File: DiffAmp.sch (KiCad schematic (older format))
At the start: 81 parts, among them J1 USB_OTG, J2 Conn_01x01_Female, J3 Conn_01x01_Female, J4 Conn_01x01_Female, J5 CONN_01X05, J6 Conn_01x01_Female, J7 Conn_01x01_Female, Q1 Q_NMOS_GSD, SW1 NR01105, U1 PIC12F1572-IMS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

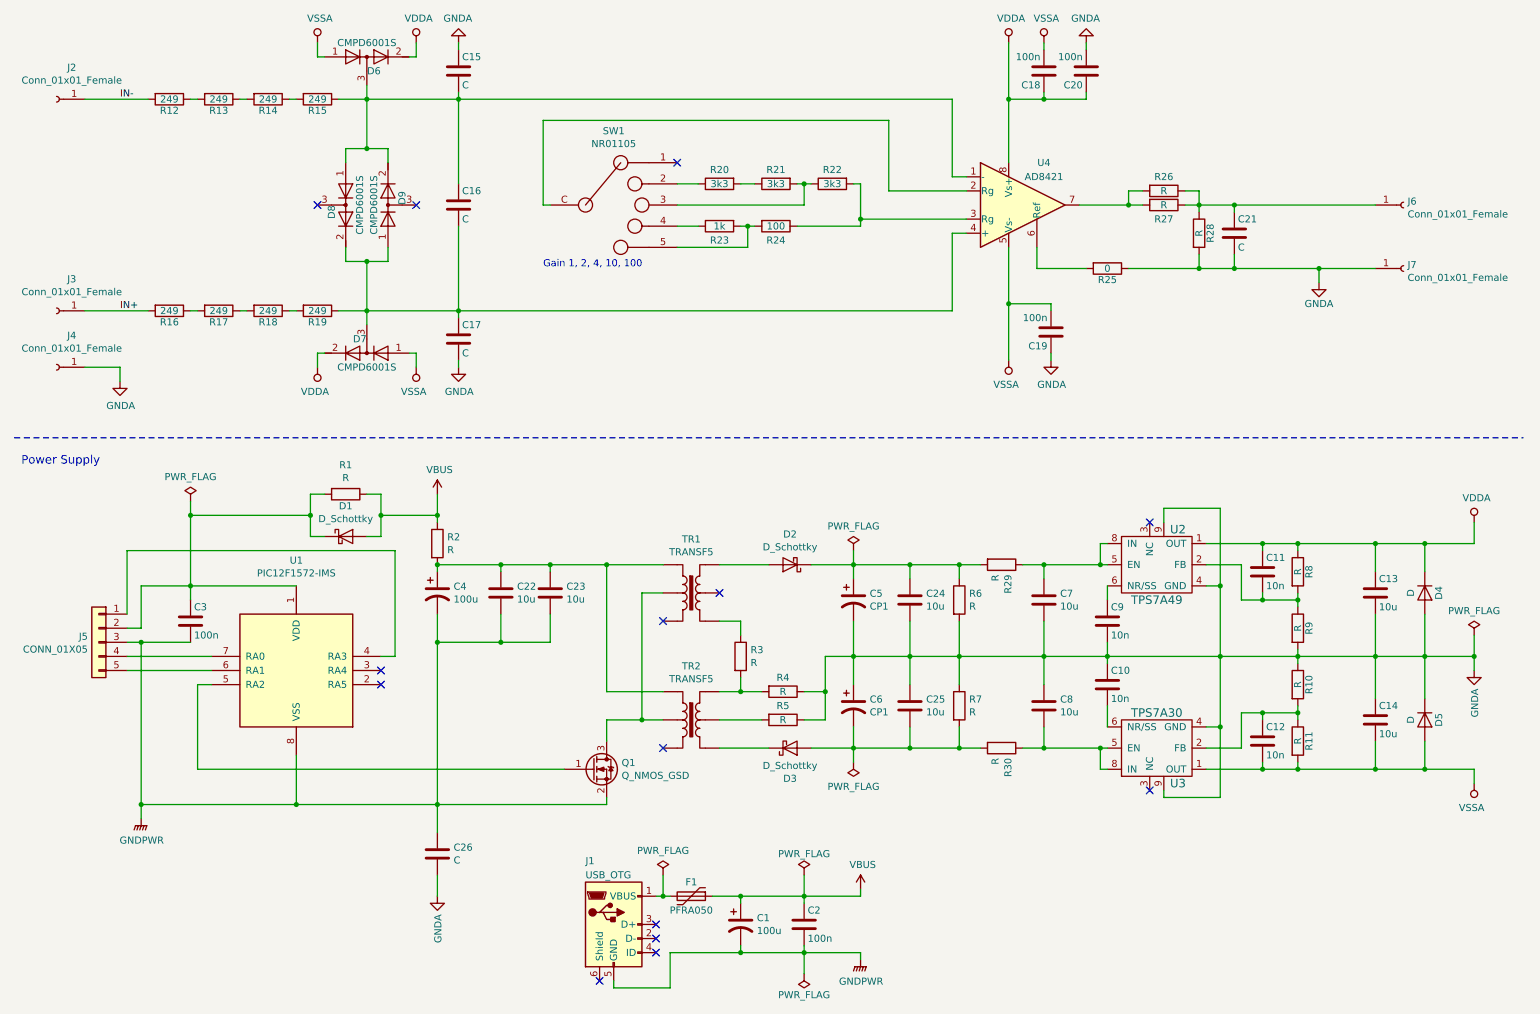
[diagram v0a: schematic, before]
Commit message: Changes in first assembly added to schematic
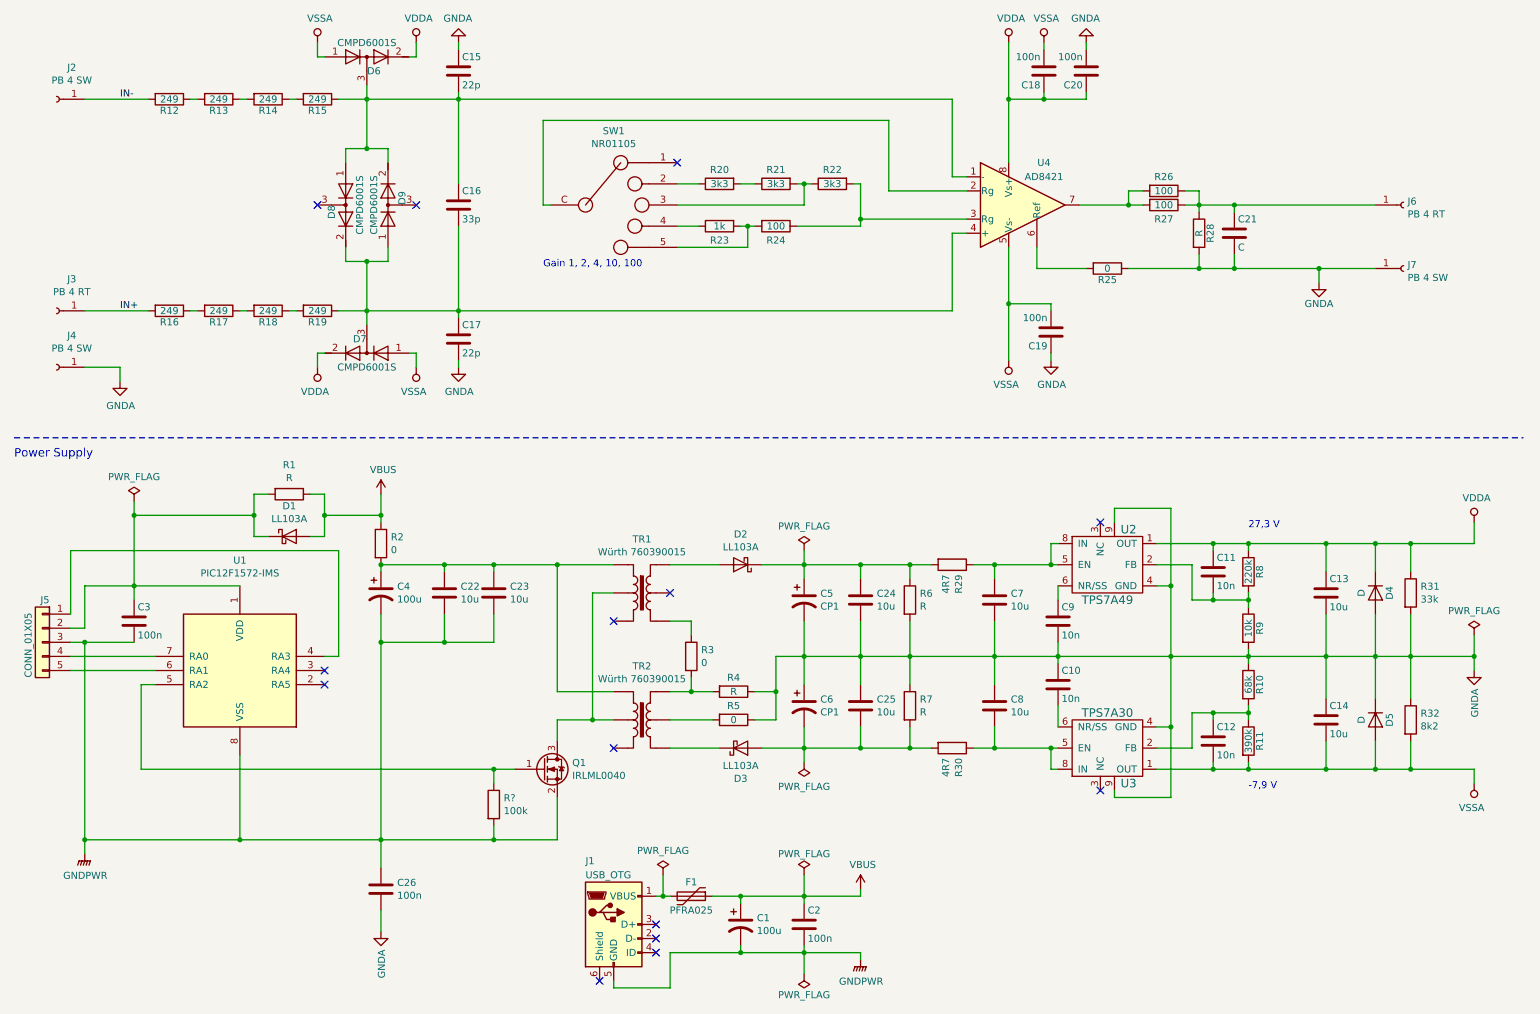
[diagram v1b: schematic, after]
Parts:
- added R31: 33k, Resistors_SMD:R_0805, symbol Device:R
- added R32: 8k2, Resistors_SMD:R_0805, symbol Device:R
- added R?: 100k, Resistors_SMD:R_0805, symbol Device:R
- C15, C17: value C -> 22p
- C16: value C -> 33p
- C26: value C -> 100n
- D1, D2, D3: value D_Schottky -> LL103A
- F1: value PFRA050 -> PFRA025
- J2, J4, J7: value Conn_01x01_Female -> PB 4 SW
- J3, J6: value Conn_01x01_Female -> PB 4 RT
- Q1: value Q_NMOS_GSD -> IRLML0040
- R10: value R -> 68k
- R11: value R -> 390k
- R2, R3, R5: value R -> 0
- R26, R27: value R -> 100
- R29, R30: value R -> 4R7
- R8: value R -> 220k
- R9: value R -> 10k
- TR1, TR2: value TRANSF5 -> Würth 760390015
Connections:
- net GNDA: now also R31.2, R32.1
- net GNDPWR: now also R?.2
- net VDDA: now also R31.1
- net VSSA: now also R32.2
- net at Q1.1 (G), U1.5 (RA2): now also R?.1
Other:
- note added: "-7,9 V"
- note added: "27,3 V"
- moved on the sheet: C10, C11, C12, C13, C14, C22, C23, C24, C25, C26, C3, C4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

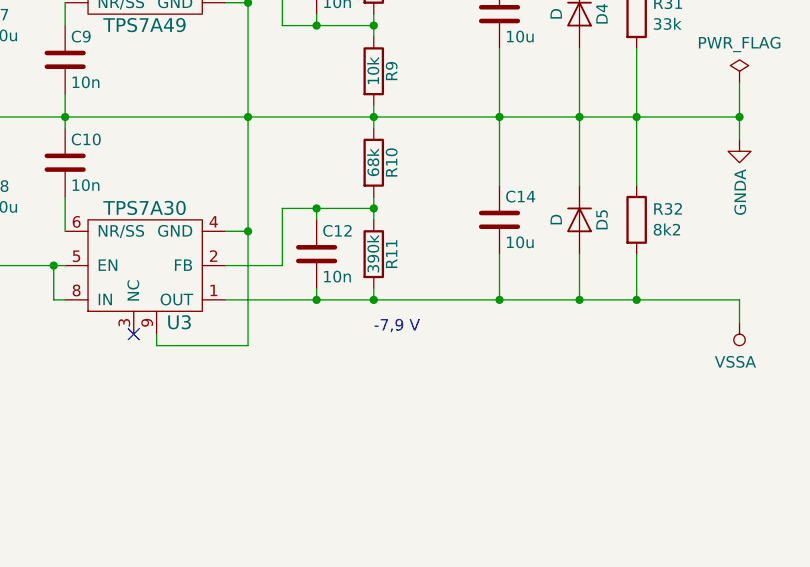
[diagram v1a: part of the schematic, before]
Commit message: Schematic revised - change in negative supply voltage
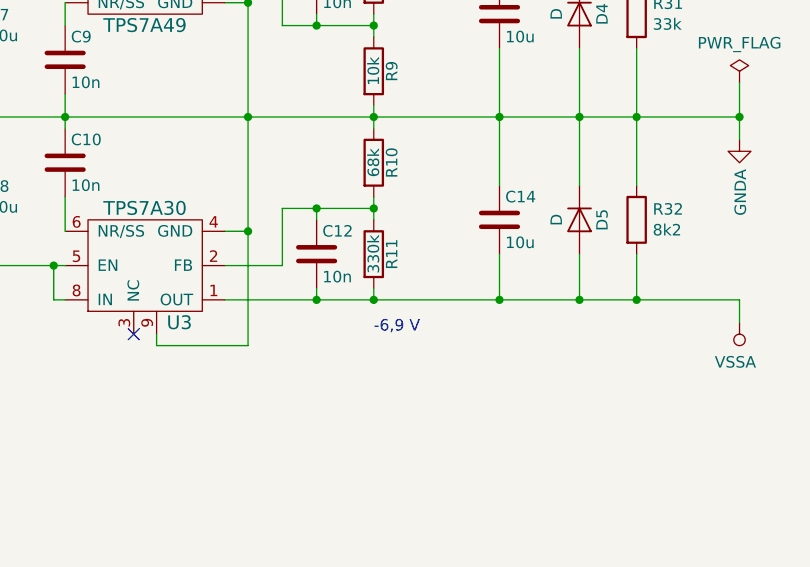
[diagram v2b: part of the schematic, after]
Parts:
- R11: value 390k -> 330k
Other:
- note added: "-6,9 V"
- note removed: "-7,9 V"
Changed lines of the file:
@@
 P 9250 5800
 F 0 "R11" V 9330 5800 50  0000 C CNN
-F 1 "390k" V 9250 5800 50  0000 C CNN
+F 1 "330k" V 9250 5800 50  0000 C CNN
 F 2 "Resistors_SMD:R_0805" V 9180 5800 50  0001 C CNN
 F 3 "" H 9250 5800 50  0001 C CNN
@@
 27,3 V
 Text Notes 9250 6150 0    50   ~ 0
--7,9 V
+-6,9 V
 $Comp
 L Connector:Conn_01x01_Female J7
